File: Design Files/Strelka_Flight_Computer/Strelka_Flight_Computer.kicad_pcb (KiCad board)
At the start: 4 copper layers, 124.4 x 38.4 mm, 167 parts, among them IC1 XTSD04GLGEAG, IC2 MAX-M10S-00B, J1 1S_LiPo_LARGE_HOLE_XT-30, J2 Conn_01x04, J3 DB125-3.5-4P-GN-S, J4 SM06B-GHS-TB(LF)(SN), J5 USB_B_Micro, J6 USB_B_Micro, Q1 ??, Q10 AP2300, Q11 MMBT2222, Q2 ??, Q3 AO3401A, Q4 AO3401A, Q5 AP2300, Q6 MMBT2222, Q8 AO3401A, Q9 AO3401A, SW1 SW_Push, SW2 SW_Push, SW3 SW_DIP_x01, U10 LM321, U11 BMX055, U12 MS561101BA03-50, U15 LM321, U16 TPS61085DGKR, U2 AP9101CK6, U3 AMS1117-3.3, U4 RFM95W-915S2, U5 STM32F405RGTx, U7 USBLC6-2SC6, U8 USBLC6-2SC6, U9 CP2102N-Axx-xQFN28, Y1 Q13FC1350000200, Y2 X322524MOB4SI

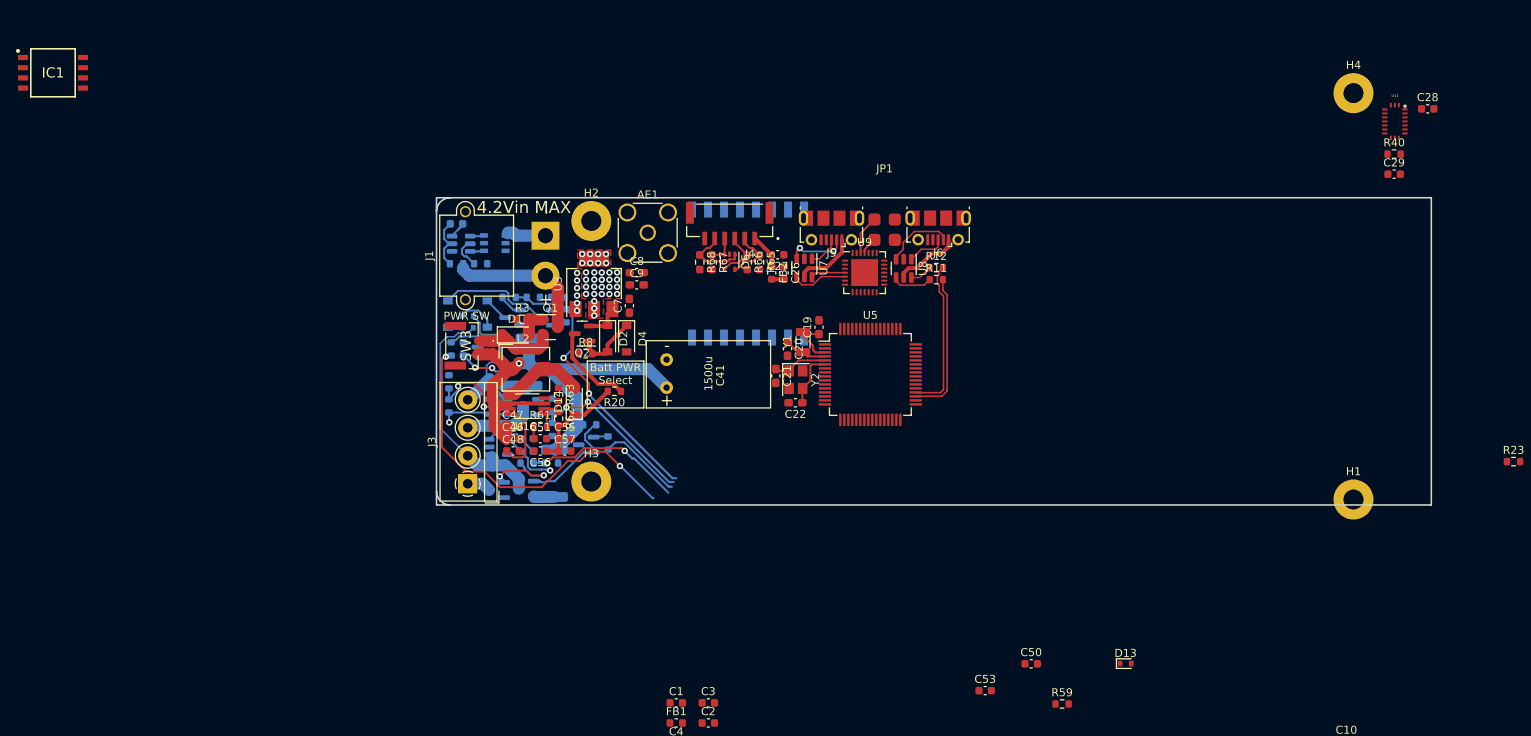
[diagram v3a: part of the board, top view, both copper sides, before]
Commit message: Power routing finished
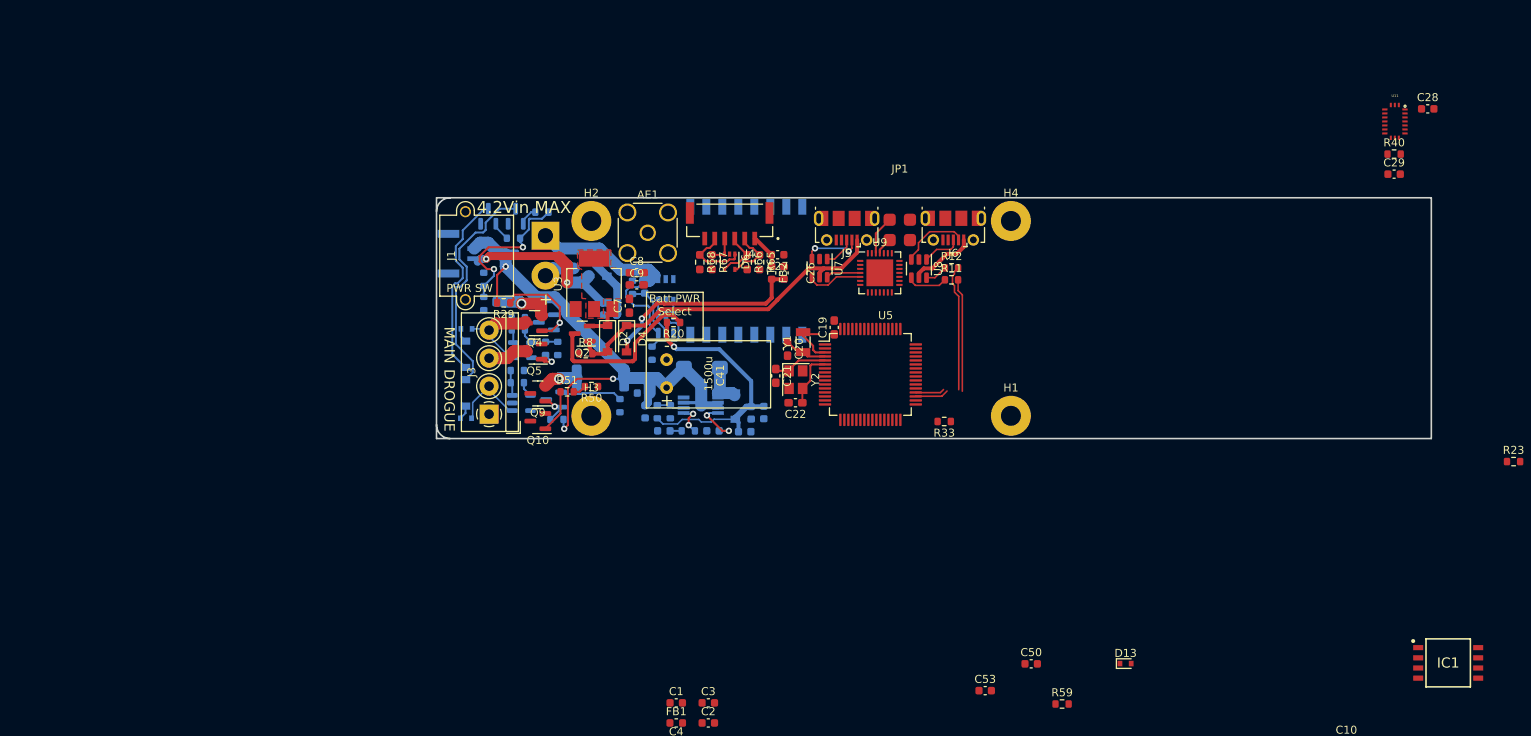
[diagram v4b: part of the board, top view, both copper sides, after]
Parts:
- C46, C47, C48, C51, C55, C56, C57, D1, D14, Q1, R3, R61, R62, R63, SW3, U16: moved to B.Cu
- Ld: renamed from L2; moved to B.Cu
- Q10, Q4, Q5, Q9, R29, R33, R50, R51: moved to F.Cu
- moved IC1 189.4 mm to (222.7, 129.6)
- moved R33 62.3 mm to (159.7, 99.5), turned to 180 degrees
- moved H4 45.7 mm to (168.0, 74.4)
- moved H1 44.1 mm to (168.0, 98.8)
- moved C56 28.3 mm to (137.1, 98.3), turned to -90 degrees
- moved U2 27.5 mm to (124.9, 87.3), turned to -90 degrees
- moved C48 25.1 mm to (130.8, 100.6), turned to 180 degrees
- moved C6 24.8 mm to (122.2, 82.7), turned to 90 degrees
- moved R9 24.2 mm to (123.1, 90.9), turned to -90 degrees
- moved C57 23.8 mm to (135.5, 98.4), turned to -90 degrees
- moved C55 22.5 mm to (134.7, 100.7)
- moved R7 22.2 mm to (120.7, 82.7), turned to -90 degrees
- moved MOSFET1 22.2 mm to (124.9, 83.0), turned to -90 degrees
- moved Ld 22.0 mm to (129.4, 92.8)
- moved U16 21.7 mm to (129.2, 97.4), turned to 0 degrees
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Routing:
- net /Actuators/DROGUE_H: track 45.1 -> 0.00 mm, vias 2 -> 0
- net /Actuators/DROGUE_CONT: track 36.8 -> 1.93 mm, vias 1 -> 0
- net VBUS: track 24.4 -> 52.0 mm
- net +5VD: track 1.55 -> 26.2 mm, vias 0 -> 2
- net +5VA: track 12.6 -> 34.6 mm, vias 0 -> 1
- net /Actuators/MAIN_CONT: track 23.7 -> 1.93 mm, vias 1 -> 0
- net /Actuators/Ematch_Main/EMATCH+: track 30.3 -> 9.37 mm
- net Net-(I1-Pad1): track 3.11 -> 23.6 mm
- net -BATT: track 7.79 -> 28.0 mm
- net /Actuators/DROGUE_L: track 21.2 -> 1.53 mm, vias 2 -> 0
- net /Actuators/MAIN_L: track 19.9 -> 1.67 mm, vias 2 -> 0
- net /Actuators/CONT_TEST_EN: track 36.3 -> 19.6 mm
- net Net-(I2-Pad1): track 13.6 -> 28.5 mm
- net +BATT: track 17.9 -> 3.90 mm
- net /Actuators/MAIN_H: track 10.7 -> 0.00 mm
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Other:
- board size 124.4 x 38.4 mm -> 124.4 x 30.1 mm
- board text added: "DROGUE"
- board text added: "MAIN"

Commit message: redo placement
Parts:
- removed C23: 1uF, Capacitor_SMD:C_0603_1608Metric_Pad1.08x0.95mm_HandSolder
- removed J5: USB_B_Micro, Connector_USB:USB_Micro-B_Molex-105017-0001
- removed JP1: UART_Switch, Footprints:UART_Switch
- removed the JP2 at (174.4, 152.4)
- removed Ld: 6u, Inductor_SMD:L_Bourns_SRP5030T
- removed R23: 10k, Resistor_SMD:R_0603_1608Metric
- removed U7: USBLC6-2SC6, Package_TO_SOT_SMD:SOT-23-6
- removed U9: CP2102N-Axx-xQFN28, Package_DFN_QFN:QFN-28-1EP_5x5mm_P0.5mm_EP3.35x3.35mm
- added L2: 6u, Inductor_SMD:L_Bourns_SRP5030T, B.Cu at (129.2, 92.8)
- added TP1: TestPoint, TestPoint:TestPoint_Pad_2.0x2.0mm, F.Cu at (148.0, 73.8)
- added TP2: TestPoint, TestPoint:TestPoint_Pad_2.0x2.0mm, F.Cu at (144.9, 73.8)
- BT2, C16, C28, C29, C31, C36, C38, D11, IC1, R14, R15, R16, R17, R18, R19, R21, R22, R35, R36, R37, R38, R39, R40, R56, U11, U12, U8: moved to B.Cu
- C55: value 68u -> 47u; footprint Capacitor_SMD:C_0603_1608Metric -> Capacitor_SMD:C_0805_2012Metric
- C56: value NC -> 47u; footprint Capacitor_SMD:C_0603_1608Metric -> Capacitor_SMD:C_0805_2012Metric
- C57: footprint Capacitor_SMD:C_0603_1608Metric -> Capacitor_SMD:C_0805_2012Metric
- J2: value Conn_01x04 -> SM04B-GHS-TB(LF)(SN)-; footprint Connector_PinHeader_2.54mm:PinHeader_1x04_P2.54mm_Horizontal -> Footprints:JST_SM04B-GHS-TB(LF)(SN)-
- Q1, Q2: value ?? -> CJK2333
- SW1, SW2: footprint Button_Switch_SMD:SW_Push_1P1T_NO_CK_KSC6xxJ -> Button_Switch_SMD:SW_Push_SPST_NO_Alps_SKRK
- SW3: value SW_DIP_x01 -> SM02B-GHS-TB(LF)(SN)
- moved SW2 116.0 mm to (183.9, 74.4), turned to 90 degrees
- moved C12 113.0 mm to (186.4, 75.5), turned to 90 degrees
- moved J2 106.9 mm to (184.7, 95.9), turned to 90 degrees
- moved C31 104.3 mm to (144.9, 96.9), turned to -90 degrees
- moved R58 103.1 mm to (169.1, 89.0), turned to 90 degrees
- moved R57 102.5 mm to (167.6, 89.0), turned to 90 degrees
- moved R39 98.5 mm to (157.8, 97.8), turned to 90 degrees
- moved C16 97.6 mm to (158.3, 81.2), turned to 90 degrees
- moved R15 97.2 mm to (159.4, 94.5), turned to 90 degrees
- moved R14 96.6 mm to (157.8, 94.5), turned to 90 degrees
- moved JP2 95.6 mm to (175.6, 92.9)
- moved R16 94.9 mm to (160.9, 94.5), turned to 90 degrees
- moved R22 94.2 mm to (166.9, 81.9), turned to -90 degrees
- moved R24 93.3 mm to (161.4, 81.1), turned to 90 degrees
- moved R36 92.2 mm to (162.5, 97.8), turned to 90 degrees
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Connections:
- J2 pad 1: GND -> /Data_Interfaces/SWCLK
- J2 pad 2: /Data_Interfaces/SWCLK -> /Data_Interfaces/SWDIO
- J2 pad 3: /Data_Interfaces/SWDIO -> GND
- R31 pad 1: Net-(Q5-Pad1) -> /Actuators/DROGUE_L
- R31 pad 2: /Actuators/DROGUE_L -> Net-(Q5-Pad1)
- R51 pad 1: Net-(Q10-Pad1) -> /Actuators/MAIN_L
- R51 pad 2: /Actuators/MAIN_L -> Net-(Q10-Pad1)
- U5 pad 42: /Data_Interfaces/RX_CP2102 -> /Data_Interfaces/RX_PAD
- U5 pad 43: /Data_Interfaces/TX_CP2102 -> /Data_Interfaces/TX_PAD
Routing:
- net VBUS: track 52.0 -> 8.09 mm
- net /Actuators/CONT_TEST_EN: track 19.6 -> 51.5 mm, vias 2 -> 4
- net /Data_Logging/CMD: track 0.00 -> 20.9 mm, vias 0 -> 2
- net +3V3: track 0.00 -> 19.5 mm, vias 0 -> 9
- net /STM32F405/USB2_IN+: track 19.5 -> 0.00 mm
- net /STM32F405/USB2_IN-: track 18.3 -> 0.00 mm
- net /Actuators/DROGUE_CONT: track 1.93 -> 17.5 mm, vias 0 -> 1
- net /Data_Logging/SD1: track 0.00 -> 14.9 mm, vias 0 -> 2
- net /Actuators/MAIN_CONT: track 1.93 -> 15.3 mm, vias 0 -> 1
- net /Data_Logging/SD0: track 0.00 -> 13.0 mm, vias 0 -> 2
- net VDC: track 70.0 -> 82.9 mm, vias 3 -> 4
- net /Data_Logging/CLK: track 0.00 -> 12.3 mm, vias 0 -> 2
- net Net-(Q6-Pad1): track 0.00 -> 11.6 mm, vias 0 -> 1
- net +BATT: track 3.90 -> 15.1 mm, vias 0 -> 2
- net /Data_Logging/SD3: track 0.00 -> 10.4 mm, vias 0 -> 2
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- added copper zone on In2.Cu, net +3V3
- added copper zone on B.Cu, net GND
- added copper zone on F.Cu, net GND
- added copper zone on In1.Cu, net GND
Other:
- board size 124.4 x 30.1 mm -> 91 x 30.1 mm

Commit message: PCB ordered
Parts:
- removed TP1, TP2: TestPoint, TestPoint:TestPoint_Pad_2.0x2.0mm
- added G***: LOGO, Footprints:Strelka_Logo, F.Cu at (154.5, 98.3)
- added G***: LOGO, Footprints:HPR_Logo, B.Cu at (151.8, 85.9)
- added TP10: TestPoint, TestPoint:TestPoint_Pad_1.0x1.0mm, F.Cu at (174.1, 100.0)
- added TP3: TestPoint, TestPoint:TestPoint_Pad_1.0x1.0mm, F.Cu at (132.1, 86.4)
- added TP4: TestPoint, TestPoint:TestPoint_Pad_1.0x1.0mm, F.Cu at (145.2, 73.9)
- added TP5: TestPoint, TestPoint:TestPoint_Pad_1.0x1.0mm, F.Cu at (111.8, 91.5)
- added TP6: TestPoint, TestPoint:TestPoint_Pad_1.0x1.0mm, F.Cu at (164.0, 85.1)
- added TP7: TestPoint, TestPoint:TestPoint_Pad_1.0x1.0mm, F.Cu at (165.6, 85.1)
- added TP8: TestPoint, TestPoint:TestPoint_Pad_1.0x1.0mm, F.Cu at (164.0, 83.5)
- added TP9: TestPoint, TestPoint:TestPoint_Pad_1.0x1.0mm, F.Cu at (176.3, 100.0)
- C13, C15, C17, C18, C30: moved to B.Cu
- moved C10 96.6 mm to (139.4, 73.4), turned to 90 degrees
- moved C30 94.4 mm to (179.2, 88.7), turned to -90 degrees
- moved C13 87.2 mm to (148.6, 94.0)
- moved C15 87.1 mm to (147.9, 77.8)
- moved C11 86.8 mm to (141.0, 73.4), turned to 90 degrees
- moved C18 83.5 mm to (147.9, 79.3)
- moved C17 76.2 mm to (144.9, 93.7), turned to 90 degrees
- moved C37 1.47 mm to (176.9, 77.5), turned to 0 degrees
- moved R33 1.46 mm to (141.6, 98.5)
- moved C14 1.12 mm to (152.9, 94.3)
- moved FB3 0.99 mm to (177.9, 75.3), turned to 180 degrees
- moved C29 0.49 mm to (172.8, 92.9)
- moved R12 0.35 mm to (160.2, 84.4)
- moved R40 0.33 mm to (172.7, 89.5)
- moved R11 0.33 mm to (162.1, 84.3)
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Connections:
- IC2 pad 9: /Sensors/GPS_RST -> /STM32F405/GPIO_PA10
- U5 pad 42: /Data_Interfaces/RX_PAD -> /915MHz_Radio/RESET_RF
- U5 pad 43: /Data_Interfaces/TX_PAD -> /STM32F405/GPIO_PA10
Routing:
- net +3V3: track 19.5 -> 159.9 mm, vias 9 -> 41
- net GND: track 4.44 -> 102.2 mm, vias 4 -> 48
- net Net-(C12-Pad2): track 0.00 -> 56.9 mm, vias 0 -> 2
- net VBUS: track 8.09 -> 64.9 mm, vias 0 -> 3
- net /STM32F405/USART2_TX: track 0.00 -> 50.7 mm, vias 0 -> 2
- net /Actuators/DROGUE_L: track 4.38 -> 54.0 mm, vias 2 -> 4
- net /Data_Interfaces/SWCLK: track 0.00 -> 48.5 mm, vias 0 -> 2
- net /STM32F405/SPI2_MISO: track 3.21 -> 50.4 mm, vias 1 -> 5
- net Net-(R10-Pad1): track 0.00 -> 45.4 mm, vias 0 -> 2
- net /Actuators/DROGUE_CONT: track 17.5 -> 62.4 mm, vias 1 -> 2
- net /STM32F405/SPI2_MOSI: track 1.50 -> 46.1 mm, vias 1 -> 5
- net /Actuators/MAIN_L: track 1.67 -> 44.5 mm, vias 0 -> 4
- net /Data_Interfaces/SWDIO: track 0.00 -> 41.4 mm, vias 0 -> 2
- net /Actuators/MAIN_CONT: track 15.3 -> 55.8 mm, vias 1 -> 2
- net /STM32F405/SPI2_NSS2: track 0.00 -> 40.1 mm, vias 0 -> 3
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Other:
- board text added: "+3.3V"
- board text added: "+5V"
- board text added: "BOOT"
- board text added: "Designed by Angus McLennan Nov 2022"
- board text added: "GPS"
- board text added: "JLCJLCJLC"
- board text added: "MISO"
- board text added: "MOSI"
- board text added: "MS5611"
- board text added: "RST"
- board text added: "RX2"
- board text added: "SCK"
- board text added: "SWD"
- board text added: "TX2"
- board text added: "UART SW"
